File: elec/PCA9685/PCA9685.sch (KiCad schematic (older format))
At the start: 13 parts

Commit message: fin v1 PCA et main carte
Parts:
- added D?: LED, symbol Device:LED
- added J?: capt_IR_1.1, symbol Connector_Generic:Conn_01x03
- added J?: capt_IR_1.2, symbol Connector_Generic:Conn_01x03
- added J?: capt_IR_1.3, symbol Connector_Generic:Conn_01x03
- added J?: capt_IR_2.1, symbol Connector_Generic:Conn_01x03
- added J?: capt_IR_2.2, symbol Connector_Generic:Conn_01x03
- added J?: capt_IR_2.3, symbol Connector_Generic:Conn_01x03
- added R?: R, symbol Device:R
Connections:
- net +5V: now also J?.1 (Pin_1), J?.1 (Pin_1), J?.1 (Pin_1), J?.1 (Pin_1), J?.1 (Pin_1), J?.1 (Pin_1), R?.1
- net GND: now also D?.1 (K), J?.2 (Pin_2), J?.2 (Pin_2), J?.2 (Pin_2), J?.2 (Pin_2), J?.2 (Pin_2), J?.2 (Pin_2)
- net outIR_1.1: now reaches U?.1 (A0)
- net outIR_1.1: now also J?.3 (Pin_3)
- net outIR_1.2: now reaches U?.2 (A1)
- net outIR_1.2: now also J?.3 (Pin_3)
- net outIR_2.3: now reaches U?.24 (A5)
- net outIR_2.3: now also J?.3 (Pin_3)
- net outIR_1.3: now reaches U?.3 (A2)
- net outIR_1.3: now also J?.3 (Pin_3)
- net outIR_2.1: now reaches U?.4 (A3)
- net outIR_2.1: now also J?.3 (Pin_3)
- net outIR_2.2: now reaches U?.5 (A4)
- net outIR_2.2: now also J?.3 (Pin_3)
- new net: D?.2 (A), R?.2
- no-connect marks 16 -> 10

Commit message: fin sch carte principale
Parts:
- removed J?: capt_IR_1.1, symbol Connector_Generic:Conn_01x03
- removed J?: capt_IR_1.2, symbol Connector_Generic:Conn_01x03
- removed J?: capt_IR_1.3, symbol Connector_Generic:Conn_01x03
- removed J?: capt_IR_2.1, symbol Connector_Generic:Conn_01x03
- removed J?: capt_IR_2.2, symbol Connector_Generic:Conn_01x03
- removed J?: capt_IR_2.3, symbol Connector_Generic:Conn_01x03
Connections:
- net +5V: now also J?.2 (Pin_2); no longer J?.1 (Pin_1)
- net GND: now also J?.1 (Pin_1), U?.23 (~OE), U?.25 (EXTCLK); no longer J?.2 (Pin_2)
- net outIR_1.1: no longer names the net of U?.1 (A0)
- net outIR_1.2: no longer names the net of U?.2 (A1)
- net outIR_1.3: no longer names the net of U?.3 (A2)
- net outIR_2.1: no longer names the net of U?.4 (A3)
- net outIR_2.2: no longer names the net of U?.5 (A4)
- net outIR_2.3: no longer names the net of U?.24 (A5)
- no-connect marks 10 -> 8

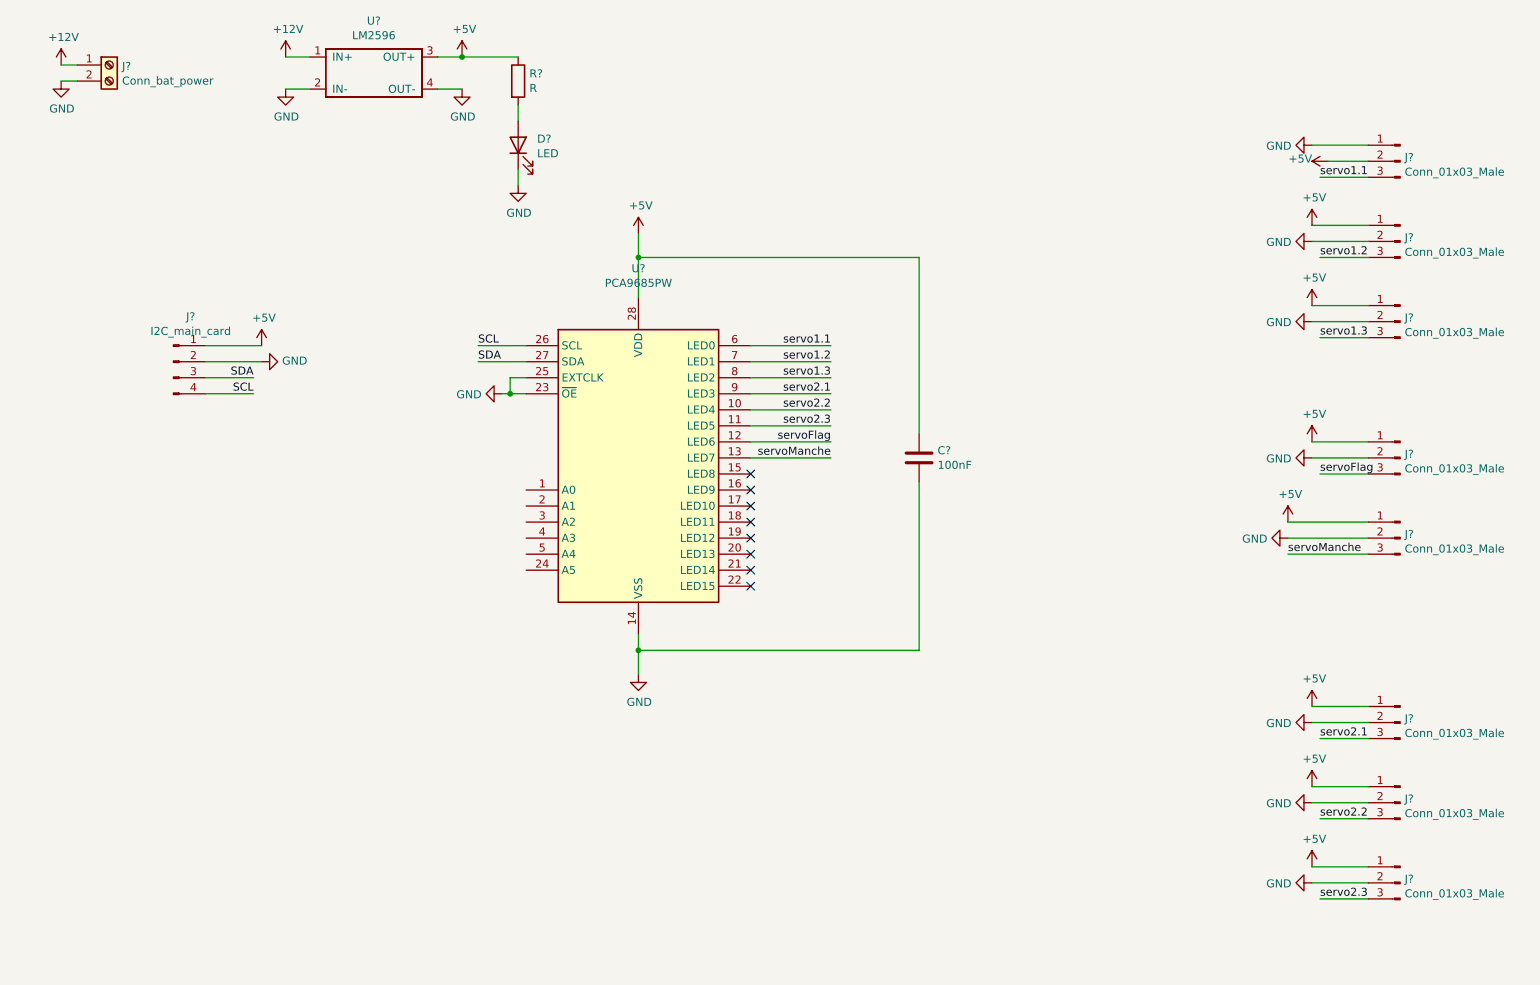
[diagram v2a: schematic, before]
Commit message: empreintes carte PAC9685
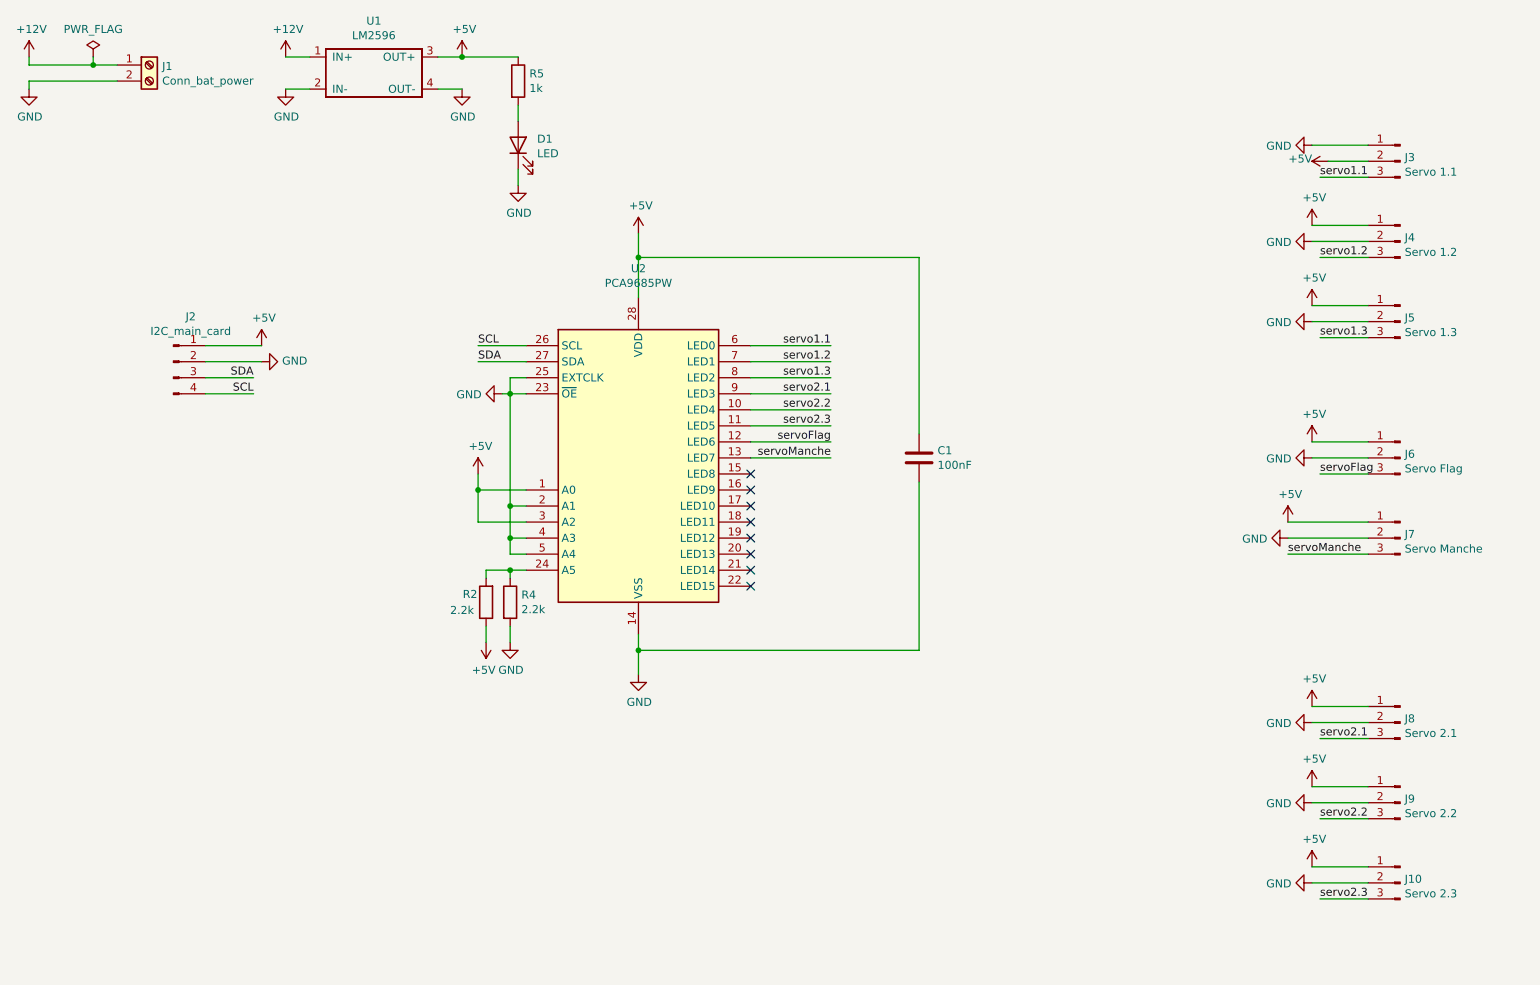
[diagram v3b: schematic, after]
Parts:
- added R2, R4: 2.2k, Resistor_SMD:R_0805_2012Metric_Pad1.15x1.40mm_HandSolder, symbol Device:R
- C1: renamed from C?; footprint (none) -> Capacitor_SMD:C_0805_2012Metric_Pad1.15x1.40mm_HandSolder
- D1: renamed from D?; footprint (none) -> LED_SMD:LED_0603_1608Metric_Pad1.05x0.95mm_HandSolder
- J1: renamed from J?; footprint (none) -> TerminalBlock:TerminalBlock_bornier-2_P5.08mm
- J10: renamed from J?; value Conn_01x03_Male -> Servo 2.3; footprint (none) -> Connector_JST:JST_XH_B3B-XH-A_1x03_P2.50mm_Vertical
- J2: renamed from J?; footprint (none) -> Connector_JST:JST_XH_B4B-XH-A_1x04_P2.50mm_Vertical
- J3: renamed from J?; value Conn_01x03_Male -> Servo 1.1; footprint (none) -> Connector_JST:JST_XH_B3B-XH-A_1x03_P2.50mm_Vertical
- J4: renamed from J?; value Conn_01x03_Male -> Servo 1.2; footprint (none) -> Connector_JST:JST_XH_B3B-XH-A_1x03_P2.50mm_Vertical
- J5: renamed from J?; value Conn_01x03_Male -> Servo 1.3; footprint (none) -> Connector_JST:JST_XH_B3B-XH-A_1x03_P2.50mm_Vertical
- J6: renamed from J?; value Conn_01x03_Male -> Servo Flag; footprint (none) -> Connector_JST:JST_XH_B3B-XH-A_1x03_P2.50mm_Vertical
- J7: renamed from J?; value Conn_01x03_Male -> Servo Manche; footprint (none) -> Connector_JST:JST_XH_B3B-XH-A_1x03_P2.50mm_Vertical
- J8: renamed from J?; value Conn_01x03_Male -> Servo 2.1; footprint (none) -> Connector_JST:JST_XH_B3B-XH-A_1x03_P2.50mm_Vertical
- J9: renamed from J?; value Conn_01x03_Male -> Servo 2.2; footprint (none) -> Connector_JST:JST_XH_B3B-XH-A_1x03_P2.50mm_Vertical
- R5: renamed from R?; value R -> 1k; footprint (none) -> Resistor_SMD:R_0805_2012Metric_Pad1.15x1.40mm_HandSolder
- U1: renamed from U?; footprint (none) -> myFootprints:LM2596
- gave numbers to parts that had none: 1
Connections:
- net +5V: now also U2.1 (A0), U2.3 (A2), R2.1
- net GND: now also U2.2 (A1), U2.4 (A3), U2.5 (A4), R4.2
- net at U2.24 (A5): now also R2.2, R4.1
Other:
- moved on the sheet: J1
